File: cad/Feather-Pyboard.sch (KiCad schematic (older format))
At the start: 39 parts, among them P1 CONN_01X16, P2 CONN_01X02, P3 CONN_01X12, P4 USB_OTG, SW1 RST, U1 SPX3819, U2 MCP73811T-420I/OT, U3 STM32F411CEUx, U4 MicroSD_SPI_CD, Y1 32.768Hz, Y2 8MHz

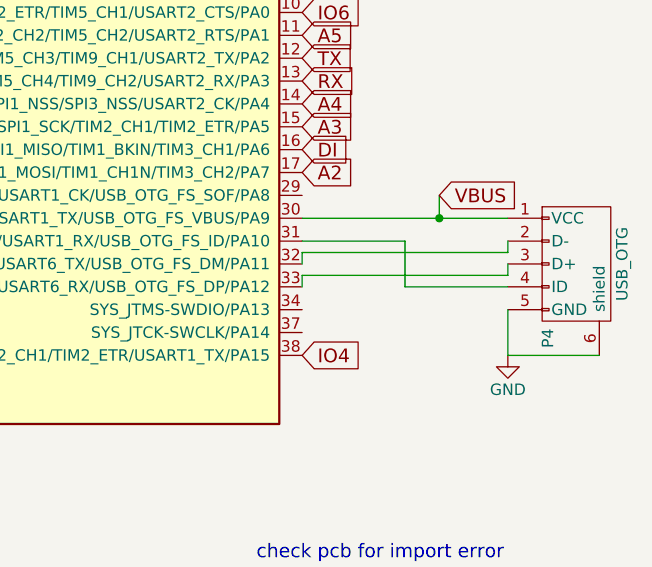
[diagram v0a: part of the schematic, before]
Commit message: new crystal footrpints and 22 ohm resistors for usb
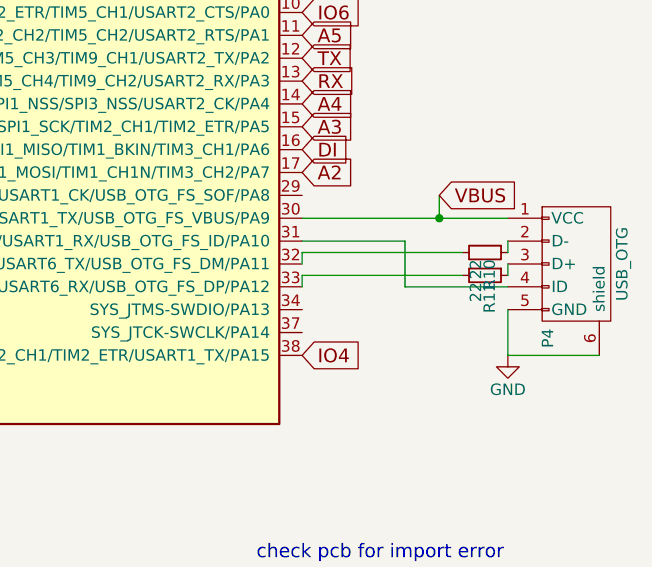
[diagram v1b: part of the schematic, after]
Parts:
- added R10, R11: 22, Resistors_SMD:R_0402, symbol R_Small
- Y1: footprint smt:R-1206 -> smt:R-0805
- Y2: footprint smt:R-1210 -> Crystals:Crystal_SMD_ABM3B
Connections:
- net at U3.32 (ADC1_EXTI11/SPI4_MISO/TIM1_CH4/USART1_CTS/USART6_TX/USB_OTG_FS_DM/PA11): now also R10.2; no longer P4.2 (D-)
- net at U3.33 (SPI5_MISO/TIM1_ETR/USART1_RTS/USART6_RX/USB_OTG_FS_DP/PA12): now also R11.2; no longer P4.3 (D+)
- new net: P4.2 (D-), R10.1
- new net: P4.3 (D+), R11.1
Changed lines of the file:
@@
 F 0 "Y2" H 2900 850 50  0000 C CNN
 F 1 "8MHz" H 2900 650 50  0000 C CNN
-F 2 "smt:R-1210" H 2900 750 50  0001 C CNN
+F 2 "Crystals:Crystal_SMD_ABM3B" H 2900 750 50  0001 C CNN
 F 3 "" H 2900 750 50  0000 C CNN
 	1    2900 750
@@
 F 0 "Y1" H 1300 850 50  0000 C CNN
 F 1 "32.768Hz" H 1300 650 50  0000 C CNN
-F 2 "smt:R-1206" H 1300 750 50  0001 C CNN
+F 2 "smt:R-0805" H 1300 750 50  0001 C CNN
 F 3 "" H 1300 750 50  0000 C CNN
 	1    1300 750
@@
 $EndComp
 $Comp
-L +3.3V #PWR01
+L +3.3V #PWR16
 U 1 1 58109C43
 P 5550 1100
-F 0 "#PWR01" H 5550 950 50  0001 C CNN
+F 0 "#PWR16" H 5550 950 50  0001 C CNN
 F 1 "+3.3V" H 5550 1240 50  0000 C CNN
 F 2 "" H 5550 1100 50  0000 C CNN
@@
 $EndComp
 $Comp
-L GND #PWR02
+L GND #PWR19
 U 1 1 58109D06
 P 7150 900
-F 0 "#PWR02" H 7150 650 50  0001 C CNN
+F 0 "#PWR19" H 7150 650 50  0001 C CNN
 F 1 "GND" H 7150 750 50  0000 C CNN
 F 2 "" H 7150 900 50  0000 C CNN
@@
 $EndComp
 $Comp
-L GND #PWR03
+L GND #PWR17
 U 1 1 5810A19E
 P 5750 5100
-F 0 "#PWR03" H 5750 4850 50  0001 C CNN
+F 0 "#PWR17" H 5750 4850 50  0001 C CNN
 F 1 "GND" H 5750 4950 50  0000 C CNN
 F 2 "" H 5750 5100 50  0000 C CNN
@@
 OSC32OUT
 $Comp
-L GND #PWR04
+L GND #PWR5
 U 1 1 5810BF33
 P 1300 1050
-F 0 "#PWR04" H 1300 800 50  0001 C CNN
+F 0 "#PWR5" H 1300 800 50  0001 C CNN
 F 1 "GND" H 1300 900 50  0000 C CNN
 F 2 "" H 1300 1050 50  0000 C CNN
@@
 $EndComp
 $Comp
-L GND #PWR05
+L GND #PWR11
 U 1 1 5810D500
 P 2900 1050
-F 0 "#PWR05" H 2900 800 50  0001 C CNN
+F 0 "#PWR11" H 2900 800 50  0001 C CNN
 F 1 "GND" H 2900 900 50  0000 C CNN
 F 2 "" H 2900 1050 50  0000 C CNN
@@
 $EndComp
 $Comp
-L +3.3V #PWR06
+L +3.3V #PWR7
 U 1 1 5810EAE7
 P 1650 1350
-F 0 "#PWR06" H 1650 1200 50  0001 C CNN
+F 0 "#PWR7" H 1650 1200 50  0001 C CNN
 F 1 "+3.3V" H 1650 1490 50  0000 C CNN
 F 2 "" H 1650 1350 50  0000 C CNN
@@
 $EndComp
 $Comp
-L GND #PWR07
+L GND #PWR3
 U 1 1 5810EB80
 P 1150 3450
-F 0 "#PWR07" H 1150 3200 50  0001 C CNN
+F 0 "#PWR3" H 1150 3200 50  0001 C CNN
 F 1 "GND" H 1150 3300 50  0000 C CNN
 F 2 "" H 1150 3450 50  0000 C CNN
@@
 AREF
 $Comp
-L +BATT #PWR08
+L +BATT #PWR6
 U 1 1 581126DD
 P 1400 5600
-F 0 "#PWR08" H 1400 5450 50  0001 C CNN
+F 0 "#PWR6" H 1400 5450 50  0001 C CNN
 F 1 "+BATT" H 1400 5740 50  0000 C CNN
 F 2 "" H 1400 5600 50  0000 C CNN
@@
 $EndComp
 $Comp
-L +5V #PWR09
+L +5V #PWR4
 U 1 1 58112721
 P 1150 5600
-F 0 "#PWR09" H 1150 5450 50  0001 C CNN
+F 0 "#PWR4" H 1150 5450 50  0001 C CNN
 F 1 "+5V" H 1150 5740 50  0000 C CNN
 F 2 "" H 1150 5600 50  0000 C CNN
@@
 $EndComp
 $Comp
-L GND #PWR010
+L GND #PWR1
 U 1 1 5811370C
 P 1000 6350
-F 0 "#PWR010" H 1000 6100 50  0001 C CNN
+F 0 "#PWR1" H 1000 6100 50  0001 C CNN
 F 1 "GND" H 1000 6200 50  0000 C CNN
 F 2 "" H 1000 6350 50  0000 C CNN
@@
 $EndComp
 $Comp
-L +3.3V #PWR011
+L +3.3V #PWR9
 U 1 1 58114400
 P 2700 6050
-F 0 "#PWR011" H 2700 5900 50  0001 C CNN
+F 0 "#PWR9" H 2700 5900 50  0001 C CNN
 F 1 "+3.3V" H 2700 6190 50  0000 C CNN
 F 2 "" H 2700 6050 50  0000 C CNN
@@
 $EndComp
 $Comp
-L GND #PWR012
+L GND #PWR10
 U 1 1 58114A56
 P 2700 6350
-F 0 "#PWR012" H 2700 6100 50  0001 C CNN
+F 0 "#PWR10" H 2700 6100 50  0001 C CNN
 F 1 "GND" H 2700 6200 50  0000 C CNN
 F 2 "" H 2700 6350 50  0000 C CNN
@@
 $EndComp
 $Comp
-L GND #PWR013
+L GND #PWR8
 U 1 1 58116AFB
 P 2550 6950
-F 0 "#PWR013" H 2550 6700 50  0001 C CNN
+F 0 "#PWR8" H 2550 6700 50  0001 C CNN
 F 1 "GND" H 2550 6800 50  0000 C CNN
 F 2 "" H 2550 6950 50  0000 C CNN
@@
 $EndComp
 $Comp
-L GND #PWR014
+L GND #PWR2
 U 1 1 58116BF4
 P 1100 7150
-F 0 "#PWR014" H 1100 6900 50  0001 C CNN
+F 0 "#PWR2" H 1100 6900 50  0001 C CNN
 F 1 "GND" H 1100 7000 50  0000 C CNN
 F 2 "" H 1100 7150 50  0000 C CNN
@@
 Connection ~ 10350 3950
 $Comp
-L GND #PWR015
+L GND #PWR22
 U 1 1 581199B4
 P 10650 4550
-F 0 "#PWR015" H 10650 4300 50  0001 C CNN
+F 0 "#PWR22" H 10650 4300 50  0001 C CNN
 F 1 "GND" H 10650 4400 50  0000 C CNN
 F 2 "" H 10650 4550 50  0000 C CNN
@@
 	10650 4050 10650 4100
 Wire Wire Line
-	10650 4100 9750 4100
-Wire Wire Line
 	9750 4100 9750 4150
 Wire Wire Line
 	9750 4250 9750 4200
-Wire Wire Line
-	9750 4200 10650 4200
 Wire Wire Line
 	10650 4200 10650 4150
@@
 CS
 $Comp
-L GND #PWR016
+L GND #PWR21
 U 1 1 5811BAA8
 P 9700 5850
-F 0 "#PWR016" H 9700 5600 50  0001 C CNN
+F 0 "#PWR21" H 9700 5600 50  0001 C CNN
 F 1 "GND" H 9700 5700 50  0000 C CNN
 F 2 "" H 9700 5850 50  0000 C CNN
@@
 	9700 5850 10500 5850
 $Comp
-L +3.3V #PWR017
+L +3.3V #PWR20
 U 1 1 5811BBFF
 P 9450 6050
-F 0 "#PWR017" H 9450 5900 50  0001 C CNN
+F 0 "#PWR20" H 9450 5900 50  0001 C CNN
 F 1 "+3.3V" H 9450 6190 50  0000 C CNN
 F 2 "" H 9450 6050 50  0000 C CNN
@@
 VBAT
 $Comp
-L GND #PWR018
+L GND #PWR15
 U 1 1 5812414D
 P 4500 6200
-F 0 "#PWR018" H 4500 5950 50  0001 C CNN
+F 0 "#PWR15" H 4500 5950 50  0001 C CNN
 F 1 "GND" H 4500 6050 50  0000 C CNN
 F 2 "" H 4500 6200 50  0000 C CNN
@@
 $EndComp
 $Comp
-L GND #PWR019
+L GND #PWR18
 U 1 1 581369A9
 P 6450 7300
-F 0 "#PWR019" H 6450 7050 50  0001 C CNN
+F 0 "#PWR18" H 6450 7050 50  0001 C CNN
 F 1 "GND" H 6450 7150 50  0000 C CNN
 F 2 "" H 6450 7300 50  0000 C CNN
@@
 RST
 $Comp
-L +3.3V #PWR020
+L +3.3V #PWR12
 U 1 1 58138F18
 P 3200 6200
-F 0 "#PWR020" H 3200 6050 50  0001 C CNN
+F 0 "#PWR12" H 3200 6050 50  0001 C CNN
 F 1 "+3.3V" H 3200 6340 50  0000 C CNN
 F 2 "" H 3200 6200 50  0000 C CNN
@@
 AREF
 $Comp
-L GND #PWR021
+L GND #PWR13
 U 1 1 58139E3F
 P 3200 6400
-F 0 "#PWR021" H 3200 6150 50  0001 C CNN
+F 0 "#PWR13" H 3200 6150 50  0001 C CNN
 F 1 "GND" H 3200 6250 50  0000 C CNN
 F 2 "" H 3200 6400 50  0000 C CNN
@@
 TX
 $Comp
-L GND #PWR022
+L GND #PWR14
 U 1 1 5813A5D0
 P 3200 7600
-F 0 "#PWR022" H 3200 7350 50  0001 C CNN
+F 0 "#PWR14" H 3200 7350 50  0001 C CNN
 F 1 "GND" H 3200 7450 50  0000 C CNN
 F 2 "" H 3200 7600 50  0000 C CNN
@@
 Text GLabel 2350 3950 0    60   Input ~ 0
 IO5
+$Comp
+L R_Small R10
+U 1 1 5819D88C
+P 10550 4100
+F 0 "R10" H 10580 4120 50  0000 L CNN
+F 1 "22" H 10580 4060 50  0000 L CNN
+F 2 "Resistors_SMD:R_0402" H 10550 4100 50  0001 C CNN
+F 3 "" H 10550 4100 50  0000 C CNN
+	1    10550 4100
+	0    1    1    0
+$EndComp
+$Comp
+L R_Small R11
+U 1 1 5819D9A8
+P 10550 4200
+F 0 "R11" H 10580 4220 50  0000 L CNN
+F 1 "22" H 10580 4160 50  0000 L CNN
+F 2 "Resistors_SMD:R_0402" H 10550 4200 50  0001 C CNN
+F 3 "" H 10550 4200 50  0000 C CNN
+	1    10550 4200
+	0    1    1    0
+$EndComp
+Wire Wire Line
+	9750 4100 10450 4100
+Wire Wire Line
+	9750 4200 10450 4200
 $EndSCHEMATC
